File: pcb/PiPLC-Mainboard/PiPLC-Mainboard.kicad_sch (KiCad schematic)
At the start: 146 parts, among them J1 WJ2EDGRC-5.08-4P, J10 WJ2EDGRC-5.08-4P, J11 WJ2EDGRC-5.08-4P, J12 WJ2EDGRC-5.08-4P, J17 Conn_02x12_Odd_Even, J2 Modbus, J3 WJ2EDGRC-5.08-4P, J4 WJ2EDGRC-5.08-4P, J5 WJ2EDGRC-5.08-4P, J6 WJ2EDGRC-5.08-4P, J7 WJ2EDGRC-5.08-4P, J8 WJ2EDGRC-5.08-4P, J9 WJ2EDGRC-5.08-4P, J99 Rpi GPIO, K1 G5RL-1A-E-TV8 DC24, K2 G5RL-1A-E-TV8 DC24, K3 G5RL-1A-E-TV8 DC24, K4 G5RL-1A-E-TV8 DC24, K5 G5RL-1A-E-TV8 DC24, K6 G5RL-1A-E-TV8 DC24, K7 G5RL-1A-E-TV8 DC24, K8 G5RL-1A-E-TV8 DC24, Q1 AO3400A, Q2 AO3400A, Q3 AO3400A, Q4 AO3400A, Q5 AO3400A, Q6 AO3400A, Q7 AO3400A, Q8 AO3400A, U1 TPS54331D, U10 EL817C, U11 EL817C, U12 ISO3082DWR, U2 NCN5121, U3 ISO1540, U4 EL817C, U5 EL817C, U6 EL817C, U7 EL817C, U8 EL817C, U9 EL817C, Y2 16MHz

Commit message: [Mainboard] Double check Pi header
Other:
- note removed: "Double quadruple check pinout! If Chris mounts this thing upside down as he currently plans to he will surely forget to flip this pinout upside down. The mere existance of this note is proof of the fact this was never checked again."
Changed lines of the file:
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@@
     (effects (font (size 1.27 1.27)) (justify left bottom))
-  )
-  (text "Double quadruple check pinout!\nIf Chris mounts this thing upside\ndown as he currently plans to\nhe will surely forget to flip\nthis pinout upside down.\nThe mere existance of this\nnote is proof of the fact\nthis was never checked again."
-    (at 214.63 95.25 0)
-    (effects (font (size 2.5 2.5)) (justify left bottom))
   )
   (text "GPIO_11" (at 219.71 135.89 0)

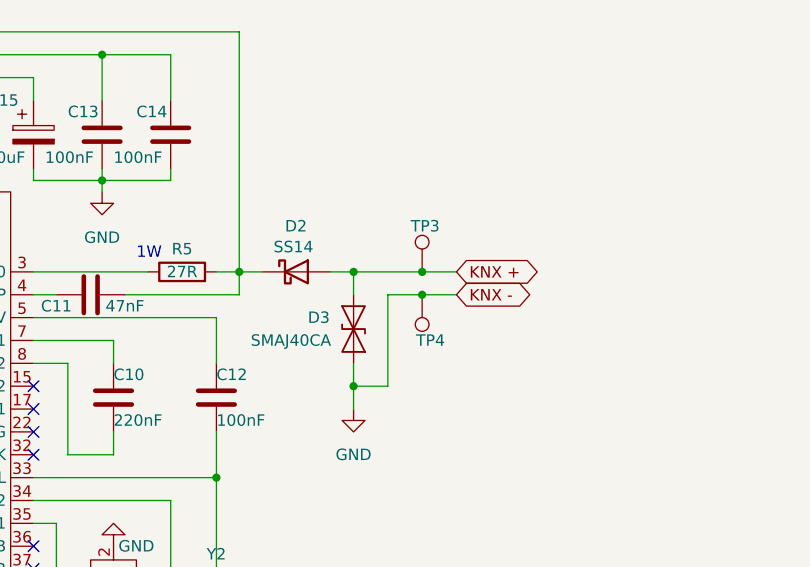
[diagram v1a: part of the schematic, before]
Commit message: You guessed it, routing
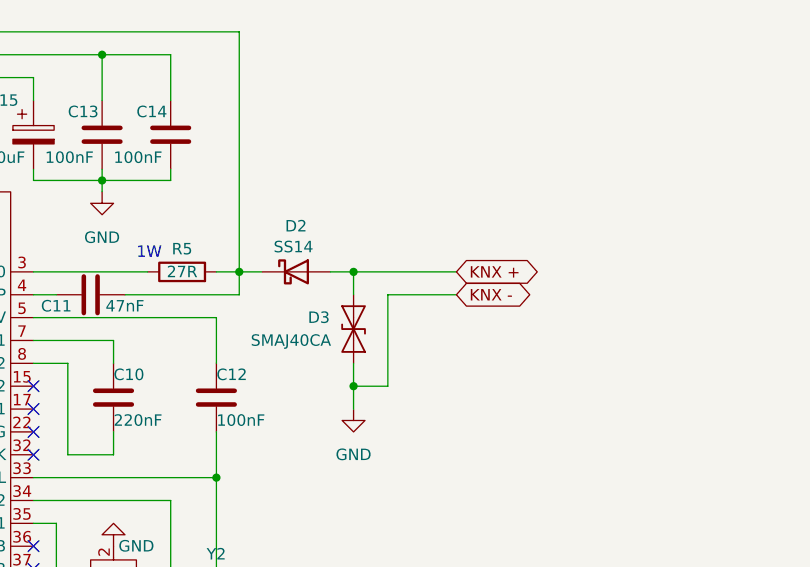
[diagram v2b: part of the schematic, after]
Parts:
- removed TP3, TP4: TestPoint, TestPoint:TestPoint_Pad_D2.0mm, symbol Connector:TestPoint
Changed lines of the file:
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@@
   (junction (at 354.33 123.19) (diameter 0) (color 0 0 0 0)
   )
-  (junction (at 430.53 90.17) (diameter 0) (color 0 0 0 0)
-  )
   (junction (at 311.15 312.42) (diameter 0) (color 0 0 0 0)
   )
@@
   (junction (at 374.65 138.43) (diameter 0) (color 0 0 0 0)
   )
-  (junction (at 430.53 92.71) (diameter 0) (color 0 0 0 0)
-  )
   (junction (at 231.14 138.43) (diameter 0) (color 0 0 0 0)
   )
@@
     (stroke (width 0) (type default))
   )
-  (wire (pts (xy 426.72 92.71) (xy 430.53 92.71))
+  (wire (pts (xy 426.72 92.71) (xy 434.34 92.71))
     (stroke (width 0) (type default))
   )
@@
     (stroke (width 0) (type default))
   )
-  (wire (pts (xy 430.53 90.17) (xy 434.34 90.17))
-    (stroke (width 0) (type default))
-  )
   (wire (pts (xy 396.24 138.43) (xy 396.24 140.97))
     (stroke (width 0) (type default))
@@
     (stroke (width 0) (type default))
   )
-  (wire (pts (xy 422.91 90.17) (xy 430.53 90.17))
+  (wire (pts (xy 422.91 90.17) (xy 434.34 90.17))
     (stroke (width 0) (type default))
   )
@@
     (stroke (width 0) (type default))
   )
-  (wire (pts (xy 430.53 92.71) (xy 434.34 92.71))
-    (stroke (width 0) (type default))
-  )
   (wire (pts (xy 135.89 49.53) (xy 140.97 49.53))
     (stroke (width 0) (type default))
@@
     )
   )
-  (symbol (lib_id "Connector:TestPoint") (at 430.53 92.71 180) (unit 1)
-    (in_bom no) (on_board yes) (dnp no)
-    (property "Reference" "TP4" (at 433.07 97.79 0)
-      (effects (font (size 1.27 1.27)) (justify left))
-    )
-    (property "Value" "TestPoint" (at 427.99 94.742 0)
-      (effects (font (size 1.27 1.27)) (justify left) hide)
-    )
-    (property "Footprint" "TestPoint:TestPoint_Pad_D2.0mm" (at 425.45 92.71 0)
-      (effects (font (size 1.27 1.27)) hide)
-    )
-    (property "Datasheet" "~" (at 425.45 92.71 0)
-      (effects (font (size 1.27 1.27)) hide)
-    )
-    (property "LCSC" "~" (at 430.53 92.71 0)
-      (effects (font (size 1.27 1.27)) hide)
-    )
-    (pin "1")
-    (instances
-      (project "PiPLC-Mainboard"
-        (path "/93ebf745-625a-4d9e-8f47-45e91f30ef94"
-          (reference "TP4") (unit 1)
-        )
-      )
-    )
-  )
   (symbol (lib_id "Transistor_FET:AO3400A") (at 91.44 321.31 0) (unit 1)
     (in_bom yes) (on_board yes) (dnp no)
@@
         )
       )
-    )
-  )
-  (symbol (lib_id "Connector:TestPoint") (at 430.53 90.17 0) (unit 1)
-    (in_bom no) (on_board yes) (dnp no)
-    (property "Reference" "TP3" (at 429.26 85.09 0)
-      (effects (font (size 1.27 1.27)) (justify left))
-    )
-    (property "Value" "TestPoint" (at 433.07 88.138 0)
-      (effects (font (size 1.27 1.27)) (justify left) hide)
-    )
-    (property "Footprint" "TestPoint:TestPoint_Pad_D2.0mm" (at 435.61 90.17 0)
-      (effects (font (size 1.27 1.27)) hide)
-    )
-    (property "Datasheet" "~" (at 435.61 90.17 0)
-      (effects (font (size 1.27 1.27)) hide)
-    )
-    (property "LCSC" "~" (at 430.53 90.17 0)
-      (effects (font (size 1.27 1.27)) hide)
-    )
-    (pin "1")
-    (instances
-      (project "PiPLC-Mainboard"
-        (path "/93ebf745-625a-4d9e-8f47-45e91f30ef94"
-          (reference "TP3") (unit 1)
-        )
-      )

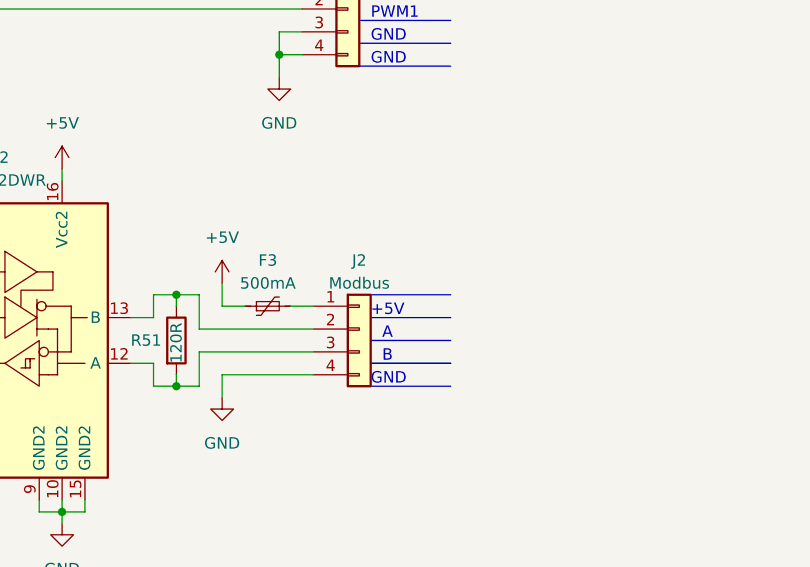
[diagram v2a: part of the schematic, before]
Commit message: [Main] Fix wrong value for Modbus plug
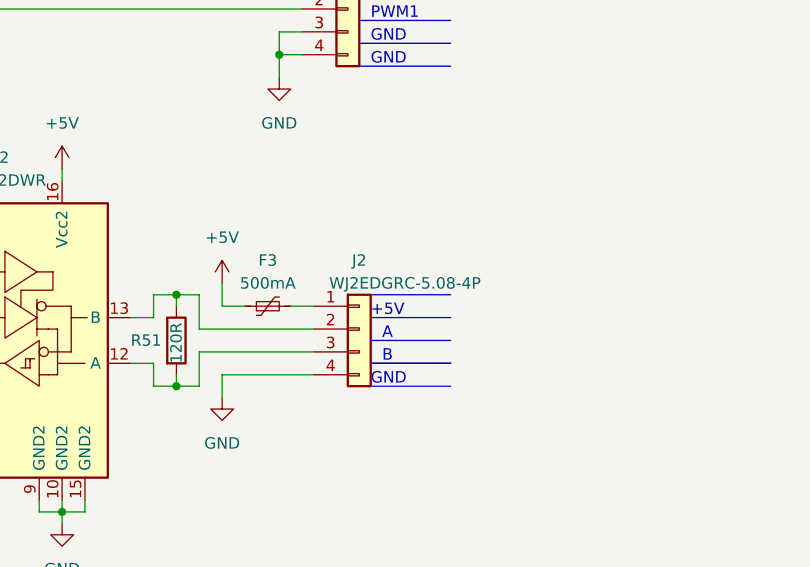
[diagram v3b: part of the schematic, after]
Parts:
- J2: value Modbus -> WJ2EDGRC-5.08-4P
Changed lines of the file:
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@@
       (effects (font (size 1.27 1.27)))
     )
-    (property "Value" "Modbus" (at 411.48 190.5 0)
+    (property "Value" "WJ2EDGRC-5.08-4P" (at 416.56 190.5 0)
       (effects (font (size 1.27 1.27)))
     )
